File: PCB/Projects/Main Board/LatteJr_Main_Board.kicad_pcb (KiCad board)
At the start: 4 copper layers, 140 x 54 mm, 133 parts, among them IC1 BQ27621YZFR-G1A, J1 Conn_01x04_Pin, J3 USB4056-03-A, J4 Conn_01x04_Pin, J5 Conn_01x04_Pin, J6 Conn_01x02_Socket, P1 RPI-RM2, Q1 BSS138DW, Q2 BSS138DW, SW1 SW_Push, SW2 SW_Push, SW3 SW_Push, SW4 SW_Push, SW5 SW_Push, SW6 SW_Push, SW7 SW_Push, SW8 SW_Push, U1 RP2350_60QFN, U10 HAL4395, U11 HAL4395, U12 HAL4395, U13 HAL4395, U14 HAL4395, U15 HAL4395, U16 HAL4395, U2 HAL4395, U3 HAL4395, U4 TPS63001DRCR, U5 BQ25180, U6 USBLC6-2P6, U7 USBLC6-2P6, U8 USBLC6-2P6, U9 HAL4395, Y1 ABM8-272-T3

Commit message: Some Routing
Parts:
- moved C26 100.5 mm to (86.4, 49.2)
- moved R24 99.9 mm to (77.8, 45.1), turned to 180 degrees
- moved R25 97.7 mm to (77.1, 44.3)
- moved R27 95.8 mm to (82.2, 47.4)
- moved R26 95.7 mm to (74.0, 42.9), turned to -90 degrees
- moved C20 93.8 mm to (75.5, 49.5), turned to 180 degrees
- moved R2 93.6 mm to (103.1, 46.6)
- moved R29 92.0 mm to (76.3, 45.1)
- moved C21 91.7 mm to (76.9, 49.5), turned to 180 degrees
- moved IC1 91.4 mm to (76.6, 47.3), turned to -90 degrees
- moved R32 90.9 mm to (95.7, 39.5), turned to -90 degrees
- moved Y1 90.9 mm to (103.0, 49.1), turned to -90 degrees
- moved R30 90.7 mm to (86.4, 48.4)
- moved Q1 90.1 mm to (93.7, 38.7), turned to 180 degrees
- moved R28 89.7 mm to (67.0, 36.8), turned to -90 degrees
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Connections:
- R22 pad 1: unconnected-(R22-Pad1) -> Net-(U1-GPIO1)
- R23 pad 1: unconnected-(R23-Pad1) -> Net-(U1-GPIO2)
- R6 pad 1: D+ -> SAFE_D+
- R7 pad 1: D- -> SAFE_D-
- R9 pad 1: unconnected-(R9-Pad1) -> Net-(U1-GPIO0)
- U1 pad 2: unconnected-(U1-GPIO0-Pad2) -> Net-(U1-GPIO0)
- U1 pad 3: unconnected-(U1-GPIO1-Pad3) -> Net-(U1-GPIO1)
- U1 pad 4: unconnected-(U1-GPIO2-Pad4) -> Net-(U1-GPIO2)
- U1 pad 44: unconnected-(U1-ADC_AVDD-Pad44) -> +3V3
- U1 pad 53: unconnected-(U1-USB_OTP_VDD-Pad53) -> +3V3
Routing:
- net VBUS: track 0.00 -> 28.2 mm, vias 0 -> 3
- net BATTERY_POS: track 0.00 -> 26.6 mm, vias 0 -> 2
- net +3.3V_PRE: track 0.00 -> 21.8 mm, vias 0 -> 2
- net N_DATA: track 0.00 -> 19.8 mm, vias 0 -> 1
- net N_CLOCK: track 0.00 -> 19.8 mm, vias 0 -> 1
- net N_LATCH: track 0.00 -> 19.4 mm, vias 0 -> 1
- net GND: track 0.00 -> 17.6 mm, vias 0 -> 6
- net SAFE_D-: track 0.00 -> 10.0 mm
- net SAFE_D+: track 0.00 -> 9.97 mm
- net D+: track 0.00 -> 9.86 mm, vias 0 -> 1
- net N_CLOCK_SAFE: track 0.00 -> 9.58 mm
- net Net-(J3-CC2): track 0.00 -> 9.50 mm, vias 0 -> 1
- net VBUS_SYS: track 0.00 -> 8.80 mm
- net D-: track 0.00 -> 8.61 mm, vias 0 -> 1
- net N_LATCH_SAFE: track 0.00 -> 7.42 mm
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
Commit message: Routing
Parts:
- removed J1: Conn_01x04_Pin, Connector_PinHeader_2.00mm:PinHeader_1x04_P2.00mm_Vertical
- removed R8: 100R, Resistor_SMD:R_0201_0603Metric
- removed the TP1 at (89.4, -14.4)
- removed the TP2 at (89.4, -11.3)
- removed TP3, TP4, TP5: TestPoint, TestPoint:TestPoint_Pad_D1.0mm
- added REF**: HHL_Logo, hhl:HHL_Logo, F.Cu at (48.0, 61.9)
- added SW9: 1TS026A-1000-0550, hhl:1TS026A-1000-0550, F.Cu at (98.3, 31.2)
- SW1: moved to B.Cu
- moved C35 120.9 mm to (154.2, 51.0), turned to 90 degrees
- moved SW1 118.6 mm to (110.9, 62.0)
- moved C28 110.7 mm to (121.4, 55.5), turned to 90 degrees
- moved R11 110.3 mm to (59.6, 56.6), turned to 180 degrees
- moved C34 109.6 mm to (150.4, 35.4), turned to 90 degrees
- moved C18 104.0 mm to (137.3, 50.8), turned to 90 degrees
- moved C29 101.0 mm to (133.5, 34.3), turned to 90 degrees
- moved R16 97.7 mm to (107.3, 47.2), turned to -90 degrees
- moved R17 96.0 mm to (108.1, 47.2), turned to -90 degrees
- moved R3 94.6 mm to (104.2, 49.4), turned to -90 degrees
- moved C30 93.0 mm to (117.7, 39.8), turned to 90 degrees
- moved R5 91.8 mm to (78.9, 47.8), turned to -90 degrees
- moved C19 91.2 mm to (52.0, 35.8), turned to 90 degrees
- moved R21 90.8 mm to (64.4, 39.8), turned to 90 degrees
- moved R4 90.3 mm to (79.8, 44.7), turned to -90 degrees
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- renumbered TP6 to TP1, TP7 to TP2
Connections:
- IC1 pad A2: I2C1_SDA -> I2C0_SDA
- IC1 pad A3: I2C1_SCL -> I2C0_SCL
- J4 pad 1: unconnected-(J4-Pin_1-Pad1) -> +3V3
- J4 pad 2: unconnected-(J4-Pin_2-Pad2) -> TRIGGER_EN_R
- J4 pad 3: unconnected-(J4-Pin_3-Pad3) -> ADC_2
- J4 pad 4: unconnected-(J4-Pin_4-Pad4) -> GND
- J5 pad 1: unconnected-(J5-Pin_1-Pad1) -> +3V3
- J5 pad 2: unconnected-(J5-Pin_2-Pad2) -> TRIGGER_EN_L
- J5 pad 3: unconnected-(J5-Pin_3-Pad3) -> ADC_1
- J5 pad 4: unconnected-(J5-Pin_4-Pad4) -> GND
- R10 pad 1: unconnected-(R10-Pad1) -> Net-(U1-GPIO4)
- R11 pad 1: unconnected-(R11-Pad1) -> Net-(U1-GPIO17)
- R12 pad 1: unconnected-(R12-Pad1) -> Net-(U1-GPIO10)
- R13 pad 1: unconnected-(R13-Pad1) -> Net-(U1-GPIO9)
- R14 pad 1: unconnected-(R14-Pad1) -> Net-(U1-GPIO15)
- R15 pad 1: unconnected-(R15-Pad1) -> Net-(U1-GPIO14)
- R16 pad 1: unconnected-(R16-Pad1) -> Net-(U1-GPIO19)
- R17 pad 1: unconnected-(R17-Pad1) -> Net-(U1-GPIO20)
- R18 pad 1: unconnected-(R18-Pad1) -> Net-(U1-GPIO24)
- R19 pad 1: unconnected-(R19-Pad1) -> Net-(U1-GPIO23)
- R20 pad 1: unconnected-(R20-Pad1) -> Net-(U1-GPIO25)
- R20 pad 2: ABXY_EN -> BTN_EN
- R21 pad 1: unconnected-(R21-Pad1) -> Net-(U1-GPIO11)
- R4 pad 2: I2C1_SCL -> I2C0_SCL
- R5 pad 1: I2C1_SDA -> I2C0_SDA
- U1 pad 10: unconnected-(U1-GPIO7-Pad10) -> WL_CS
- U1 pad 12: unconnected-(U1-GPIO8-Pad12) -> WL_CLK
- U1 pad 13: unconnected-(U1-GPIO9-Pad13) -> Net-(U1-GPIO9)
- U1 pad 14: unconnected-(U1-GPIO10-Pad14) -> Net-(U1-GPIO10)
- U1 pad 15: unconnected-(U1-GPIO11-Pad15) -> Net-(U1-GPIO11)
- U1 pad 16: unconnected-(U1-GPIO12-Pad16) -> I2C0_SDA
- U1 pad 17: unconnected-(U1-GPIO13-Pad17) -> I2C0_SCL
- U1 pad 18: unconnected-(U1-GPIO14-Pad18) -> Net-(U1-GPIO14)
- U1 pad 19: unconnected-(U1-GPIO15-Pad19) -> Net-(U1-GPIO15)
- U1 pad 28: unconnected-(U1-GPIO17-Pad28) -> Net-(U1-GPIO17)
- U1 pad 31: unconnected-(U1-GPIO19-Pad31) -> Net-(U1-GPIO19)
- U1 pad 32: unconnected-(U1-GPIO20-Pad32) -> Net-(U1-GPIO20)
- U1 pad 35: unconnected-(U1-GPIO23-Pad35) -> Net-(U1-GPIO23)
- U1 pad 36: unconnected-(U1-GPIO24-Pad36) -> Net-(U1-GPIO24)
- U1 pad 37: unconnected-(U1-GPIO25-Pad37) -> Net-(U1-GPIO25)
- U1 pad 60: unconnected-(U1-QSPI_SS-Pad60) -> USB_BOOT
- U1 pad 61: unconnected-(U1-GND-Pad61) -> GND
- U1 pad 7: unconnected-(U1-GPIO4-Pad7) -> Net-(U1-GPIO4)
- U1 pad 8: unconnected-(U1-GPIO5-Pad8) -> WL_ON
- U1 pad 9: unconnected-(U1-GPIO6-Pad9) -> WL_D
- U10 pad 5: ADC_2 -> ADC_3
- U11 pad 5: ADC_3 -> ADC_2
- U12 pad 5: ADC_1 -> ADC_2
- U13 pad 5: ADC_2 -> ADC_0
- U14 pad 5: ADC_3 -> ADC_1
- U15 pad 2: TRIGGER_EN -> TRIGGER_EN_R
- U15 pad 5: ADC_0 -> ADC_3
- U16 pad 2: TRIGGER_EN -> TRIGGER_EN_R
- U3 pad 5: unconnected-(U3-OUT-Pad5) -> ADC_3
- U5 pad B1: I2C1_SCL -> I2C0_SCL
- U5 pad C1: I2C1_SDA -> I2C0_SDA
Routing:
- net ADC_1: track 0.00 -> 169.8 mm, vias 0 -> 5
- net ADC_2: track 0.00 -> 158.9 mm, vias 0 -> 3
- net ADC_3: track 0.00 -> 143.7 mm, vias 0 -> 4
- net ADC_0: track 0.00 -> 116.7 mm, vias 0 -> 4
- net DPAD_EN: track 0.00 -> 95.8 mm, vias 0 -> 6
- net +3V3: track 4.05 -> 97.9 mm, vias 0 -> 41
- net GND: track 17.6 -> 108.3 mm, vias 6 -> 68
- net TRIGGER_EN_L: track 0.00 -> 84.8 mm, vias 0 -> 1
- net Net-(RGB4-DOUT): track 0.00 -> 82.8 mm, vias 0 -> 4
- net TRIGGER_EN_R: track 0.00 -> 75.9 mm, vias 0 -> 4
- net BTN_EN: track 0.00 -> 69.3 mm, vias 0 -> 6
- net Net-(U1-GPIO17): track 0.00 -> 56.7 mm, vias 0 -> 2
- net WL_D: track 0.00 -> 54.8 mm, vias 0 -> 3
- net WL_CLK: track 0.00 -> 52.9 mm, vias 0 -> 2
- net Net-(U1-GPIO11): track 0.00 -> 48.3 mm, vias 0 -> 2
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- added copper zone on In2.Cu, net +3V3
- added copper zone on B.Cu, net GND
- added copper zone on F.Cu, net GND
- added copper zone on In1.Cu, net GND
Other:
- board text added: "Latte Jr 11.19.2025 Designed By Mitch"

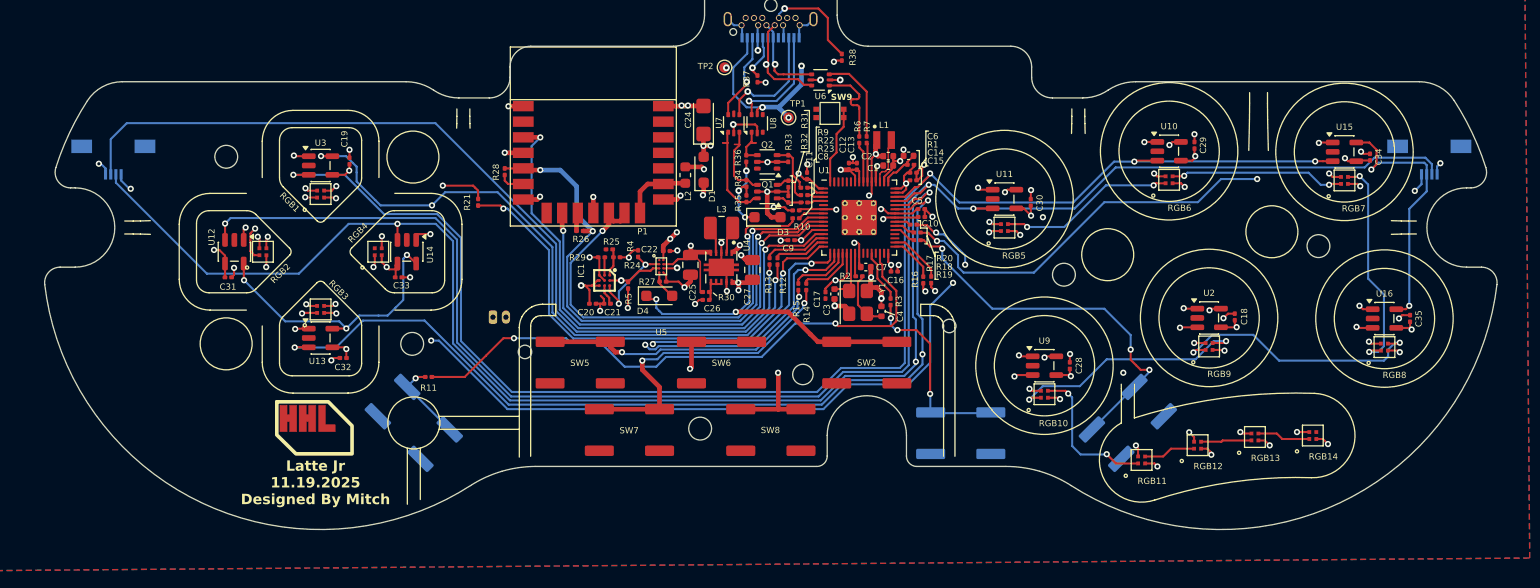
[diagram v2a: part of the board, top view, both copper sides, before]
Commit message: Main Board Routing
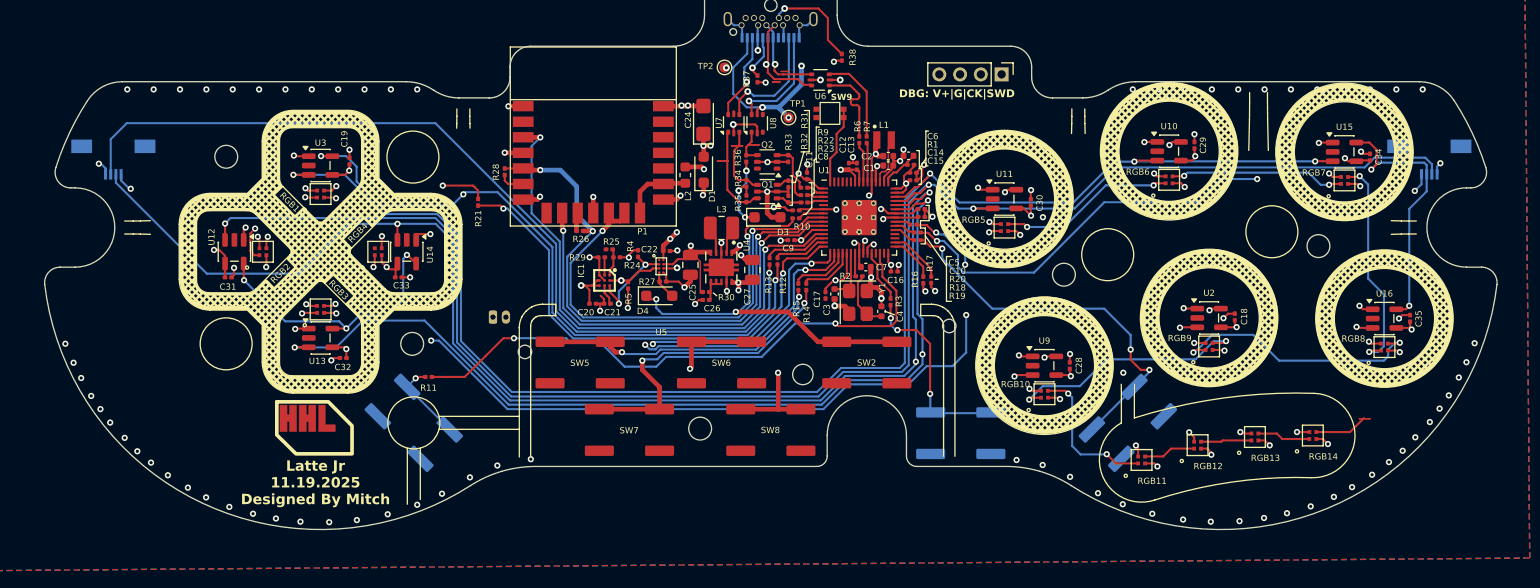
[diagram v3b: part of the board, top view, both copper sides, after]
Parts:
- added J1: Conn_01x04_Pin, Connector_PinHeader_2.00mm:PinHeader_1x04_P2.00mm_Vertical, F.Cu at (114.9, 27.4)
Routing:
- net SWD: track 0.00 -> 24.0 mm, vias 0 -> 1
- net SWCLK: track 0.00 -> 23.6 mm, vias 0 -> 1
- net VBUS: track 49.3 -> 62.5 mm
- net unconnected-(RGB14-DOUT-Pad3): track 0.00 -> 5.15 mm
- net DPAD_EN: track 95.8 -> 99.3 mm
- net Net-(RGB4-DOUT): track 82.8 -> 85.3 mm
- net GND: vias 68 -> 140
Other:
- board text added: "DBG: V+|G|CK|SWD"

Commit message: Update PCB
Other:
- outline, holes or cut-outs redrawn
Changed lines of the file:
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@@
 		(tags "resistor")
 		(property "Reference" "R34"
-			(at 0.500501 -0.789499 90)
+			(at 0.221101 -1.475299 90)
 			(layer "F.SilkS")
 			(effects
@@
 		(tags "resistor")
 		(property "Reference" "R36"
-			(at 0.083699 -0.799698 90)
+			(at -0.221101 -0.799698 90)
 			(layer "F.SilkS")
 			(effects
@@
 		(pts
 			(arc
-				(start 88.832779 34.305288)
-				(mid 89.900787 34.305288)
-				(end 88.832779 34.305288)
-			)
-		)
-		(stroke
-			(width 0)
-			(type solid)
-		)
-		(fill yes)
-		(layer "F.Cu")
-		(net 72)
-	)
-	(gr_poly
-		(pts
-			(arc
 				(start 92.772302 28.153184)
 				(mid 93.522356 28.153184)
@@
 		(pts
 			(arc
-				(start 90.407579 34.229088)
-				(mid 91.475587 34.229088)
-				(end 90.407579 34.229088)
-			)
-		)
-		(stroke
-			(width 0)
-			(type solid)
-		)
-		(fill yes)
-		(layer "F.Cu")
-		(net 76)
-	)
-	(gr_poly
-		(pts
-			(arc
 				(start 93.614446 27.148723)
 				(mid 94.3645 27.148723)
@@
 		(pts
 			(arc
-				(start 87.475884 35.7886)
-				(mid 88.543892 35.7886)
-				(end 87.475884 35.7886)
-			)
-		)
-		(stroke
-			(width 0)
-			(type solid)
-		)
-		(fill yes)
-		(layer "F.Cu")
-		(net 73)
-	)
-	(gr_poly
-		(pts
-			(arc
 				(start 149.328936 60.614915)
 				(mid 150.396944 60.614915)
@@
 		(layer "F.Mask")
 	)
+	(gr_poly
+		(pts
+			(arc
+				(start 88.832779 34.305288)
+				(mid 89.900787 34.305288)
+				(end 88.832779 34.305288)
+			)
+		)
+		(stroke
+			(width 0)
+			(type solid)
+		)
+		(fill yes)
+		(layer "F.Mask")
+	)
 	(gr_arc
 		(start 22.60309 47.722339)
@@
 		(pts
 			(arc
+				(start 90.407579 34.229088)
+				(mid 91.475587 34.229088)
+				(end 90.407579 34.229088)
+			)
+		)
+		(stroke
+			(width 0)
+			(type solid)
+		)
+		(fill yes)
+		(layer "F.Mask")
+	)
+	(gr_poly
+		(pts
+			(arc
 				(start 93.614446 27.148723)
 				(mid 94.3645 27.148723)
@@
 		(layer "F.Mask")
 	)
+	(gr_poly
+		(pts
+			(arc
+				(start 87.475884 35.7886)
+				(mid 88.543892 35.7886)
+				(end 87.475884 35.7886)
+			)
+		)
+		(stroke
+			(width 0)
+			(type solid)
+		)
+		(fill yes)
+		(layer "F.Mask")
+	)
 	(gr_line
 		(start 115.715017 24.754682)
@@
 	)
 	(gr_line
+		(start 89.2302 37.7444)
+		(end 89.8906 37.8968)
+		(stroke
+			(width 0.1)
+			(type default)
+		)
+		(layer "F.SilkS")
+	)
+	(gr_line
 		(start 62.367586 30.7594)
 		(end 62.367586 31.474235)
@@
 		(layer "Edge.Cuts")
 	)
+	(gr_circle
+		(center 140.913339 42.598349)
+		(end 142.013339 42.598349)
+		(stroke
+			(width 0.05)
+			(type default)
+		)
+		(fill no)
+		(layer "Edge.Cuts")
+	)
 	(gr_curve
 		(pts
@@
 		(layer "Edge.Cuts")
 	)
+	(gr_circle
+		(center 40.132715 53.400524)
+		(end 41.232715 53.400524)
+		(stroke
+			(width 0.05)
+			(type default)
+		)
+		(fill no)
+		(layer "Edge.Cuts")
+	)
 	(gr_curve
 		(pts
@@
 		(net 0)
 		(net_name "")
+		(layers "F.Cu" "B.Cu" "In1.Cu" "In2.Cu")
+		(hatch edge 0.5)
+		(connect_pads
+			(clearance 0)
+		)
+		(min_thickness 0.25)
+		(filled_areas_thickness no)
+		(keepout
+			(tracks allowed)
+			(vias allowed)
+			(pads allowed)
+			(copperpour not_allowed)
+			(footprints allowed)
+		)
+		(placement
+			(enabled no)
+			(sheetname "")
+		)
+		(fill
+			(thermal_gap 0.5)
+			(thermal_bridge_width 0.5)
+		)
+		(polygon
+			(pts
+				(xy 67.5386 24.7904) (xy 67.5386 29.8958) (xy 83.5152 29.8958) (xy 83.5152 24.638)
+			)
+		)
+	)
+	(zone
+		(net 0)
+		(net_name "")
 		(layer "F.SilkS")
 		(hatch none 0.5)
@@
 			(thermal_bridge_width 0.5)
 			(hatch_thickness 0.25)
-			(hatch_gap 0.25)
+			(hatch_gap 0.45)
 			(hatch_orientation 45)
 			(hatch_border_algorithm hatch_thickness)
@@
 			(thermal_bridge_width 0.5)
 			(hatch_thickness 0.25)
-			(hatch_gap 0.25)
+			(hatch_gap 0.45)
 			(hatch_orientation 45)
 			(hatch_border_algorithm hatch_thickness)
@@
 			(thermal_bridge_width 0.5)
 			(hatch_thickness 0.25)
-			(hatch_gap 0.25)
+			(hatch_gap 0.45)
 			(hatch_orientation 45)
 			(hatch_border_algorithm hatch_thickness)
@@
 			(thermal_bridge_width 0.5)
 			(hatch_thickness 0.25)
-			(hatch_gap 0.25)
+			(hatch_gap 0.45)
 			(hatch_orientation 45)
 			(hatch_border_algorithm hatch_thickness)
@@
 			(thermal_bridge_width 0.5)
 			(hatch_thickness 0.25)
-			(hatch_gap 0.25)
+			(hatch_gap 0.45)
 			(hatch_orientation 45)
 			(hatch_border_algorithm hatch_thickness)
@@
 			(thermal_bridge_width 0.5)
 			(hatch_thickness 0.25)
-			(hatch_gap 0.25)
+			(hatch_gap 0.45)
 			(hatch_orientation 45)
 			(hatch_border_algorithm hatch_thickness)
@@
 			(thermal_bridge_width 0.5)
 			(hatch_thickness 0.25)
-			(hatch_gap 0.25)
+			(hatch_gap 0.45)
 			(hatch_orientation 45)
 			(hatch_border_algorithm hatch_thickness)
@@
 			"530d4f74-5030-47f9-9c38-6b02be5f3541" "62cd1334-a46e-4220-a90c-2d0e498aa883"
 			"688db4f7-c9f4-4680-9ffa-807026b41162" "81b3b4e2-bb58-4d1f-b99f-3764c998b410"
-			"aafcaa07-27d5-4ff4-ba27-73f8f24aec5a" "b21c496b-ac95-47a3-8a63-4bec86a4c7e0"
-			"bb908577-cdd9-4a37-8dbc-670e927b9e52" "c4a72f5c-9349-48f4-8e50-22cadfdf9d5a"
-			"d235b2cd-0e1b-41ba-b760-3ded24248f8c" "eb05414a-3ccf-49bc-8603-2525d16c1ae0"
-			"f0b800fd-6ac8-4503-aeba-d3f1b598d07f" "fe376515-b4b9-4fb0-9d00-3ec2e6d52d5c"
-			"fe8c9bf4-a21e-4a5a-8a6c-b9c60439b85d"
+			"89d7b97c-b7f9-484c-ae8a-6a01f3dfe0bf" "aafcaa07-27d5-4ff4-ba27-73f8f24aec5a"
+			"b21c496b-ac95-47a3-8a63-4bec86a4c7e0" "bb908577-cdd9-4a37-8dbc-670e927b9e52"
+			"c4a72f5c-9349-48f4-8e50-22cadfdf9d5a" "d235b2cd-0e1b-41ba-b760-3ded24248f8c"
+			"eb05414a-3ccf-49bc-8603-2525d16c1ae0" "f0b800fd-6ac8-4503-aeba-d3f1b598d07f"
+			"fe376515-b4b9-4fb0-9d00-3ec2e6d52d5c" "fe8c9bf4-a21e-4a5a-8a6c-b9c60439b85d"
 		)
 	)
@@
 		)
 	)
+	(group ""
+		(members "07ed899e-87dc-4165-9bde-b9df9399927c" "bece591f-24af-4a64-8b41-d4b9e639771a")
+	)
 	(generated

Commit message: Prod
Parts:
- moved U12 0.20 mm to (41.1, 44.5)
- moved U13 0.20 mm to (49.2, 52.6)
- moved U14 0.20 mm to (57.3, 44.5)
- moved U3 0.20 mm to (49.2, 36.4)
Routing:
- net Net-(RGB1-DOUT): track 14.9 -> 14.2 mm
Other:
- board text added: "Latte Jr 11.20.2025 Designed By Mitch"
- board text removed: "Latte Jr 11.19.2025 Designed By Mitch"

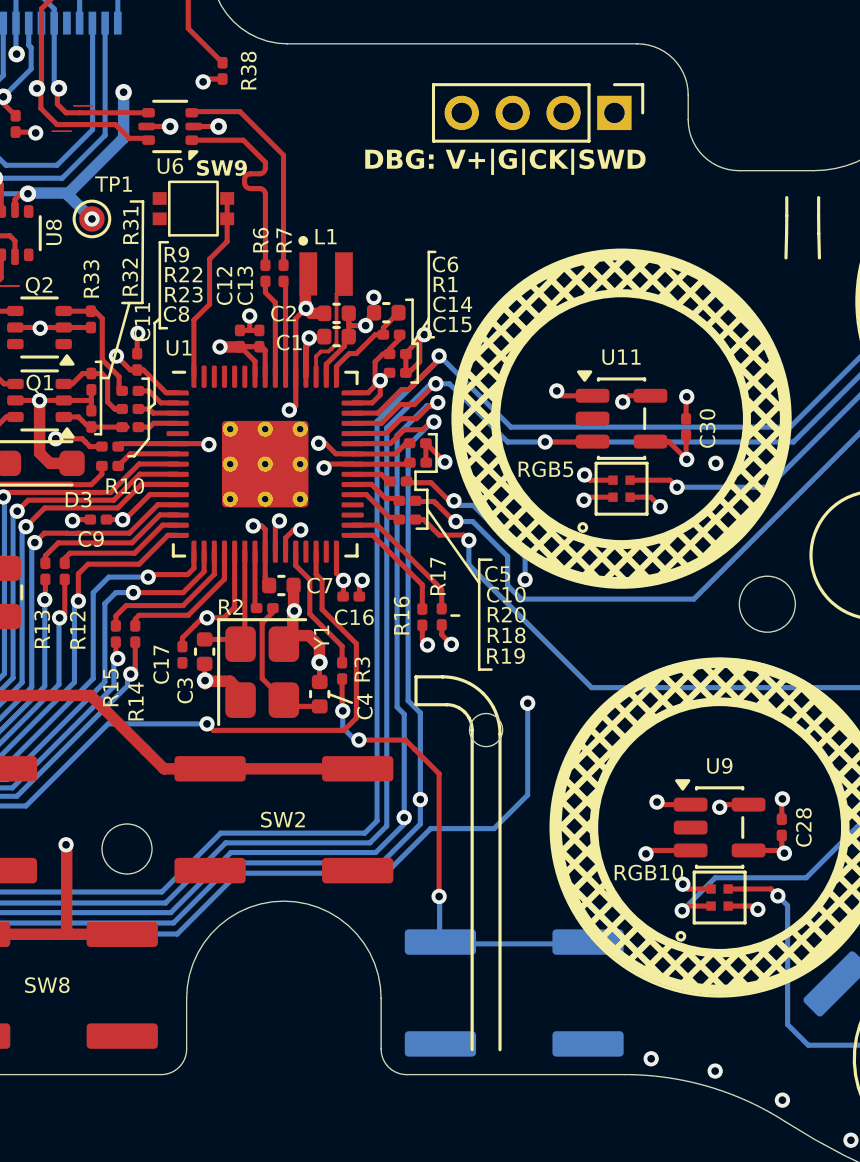
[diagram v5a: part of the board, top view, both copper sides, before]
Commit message: BOOT button placement
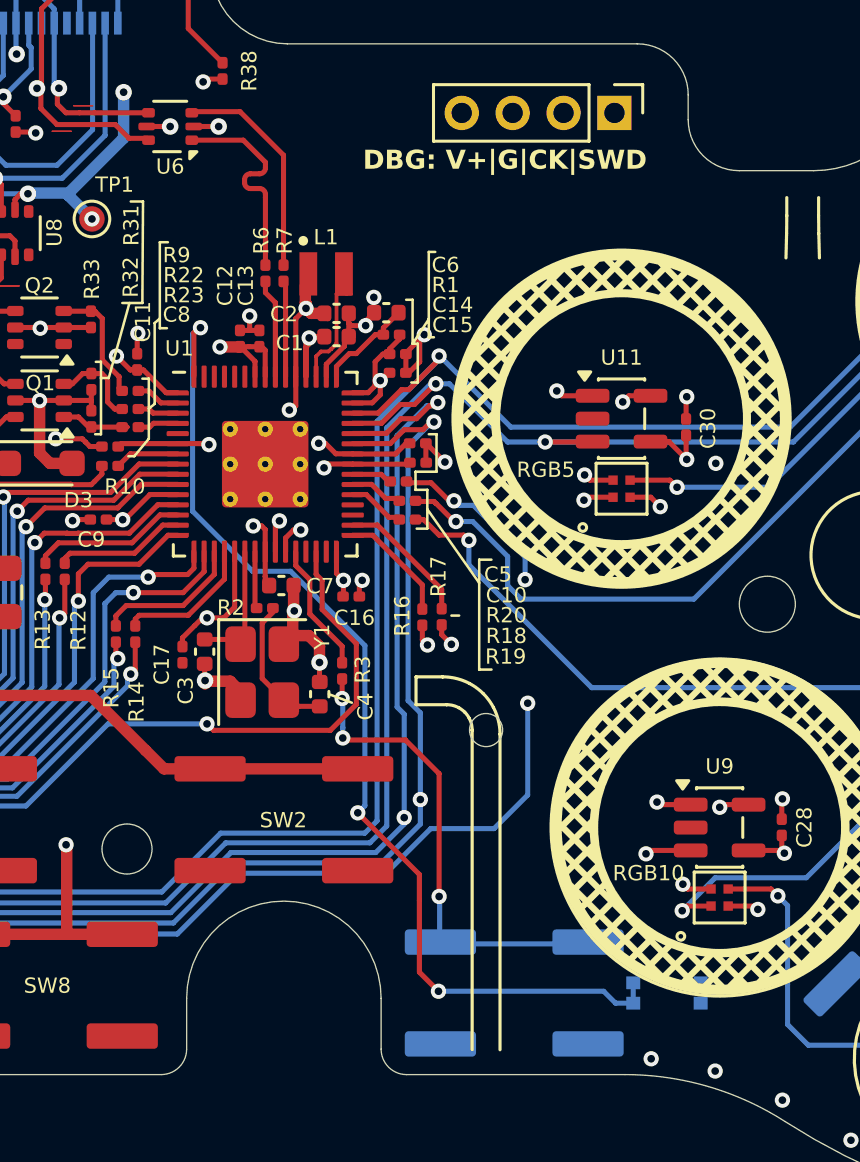
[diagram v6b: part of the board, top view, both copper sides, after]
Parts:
- SW9: moved to B.Cu
- moved SW9 36.0 mm to (116.9, 62.0)
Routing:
- net USB_BOOT: track 7.54 -> 42.0 mm, vias 0 -> 3
